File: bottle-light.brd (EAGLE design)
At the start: 88 x 88 mm, 48 parts, among them IC1 STM32F334K8T, IC2 LF33, J2 UJ2-MIBH-4-SMT-TR, U1 EC11B15242AZ, X1 78127-1128, X3 SWD

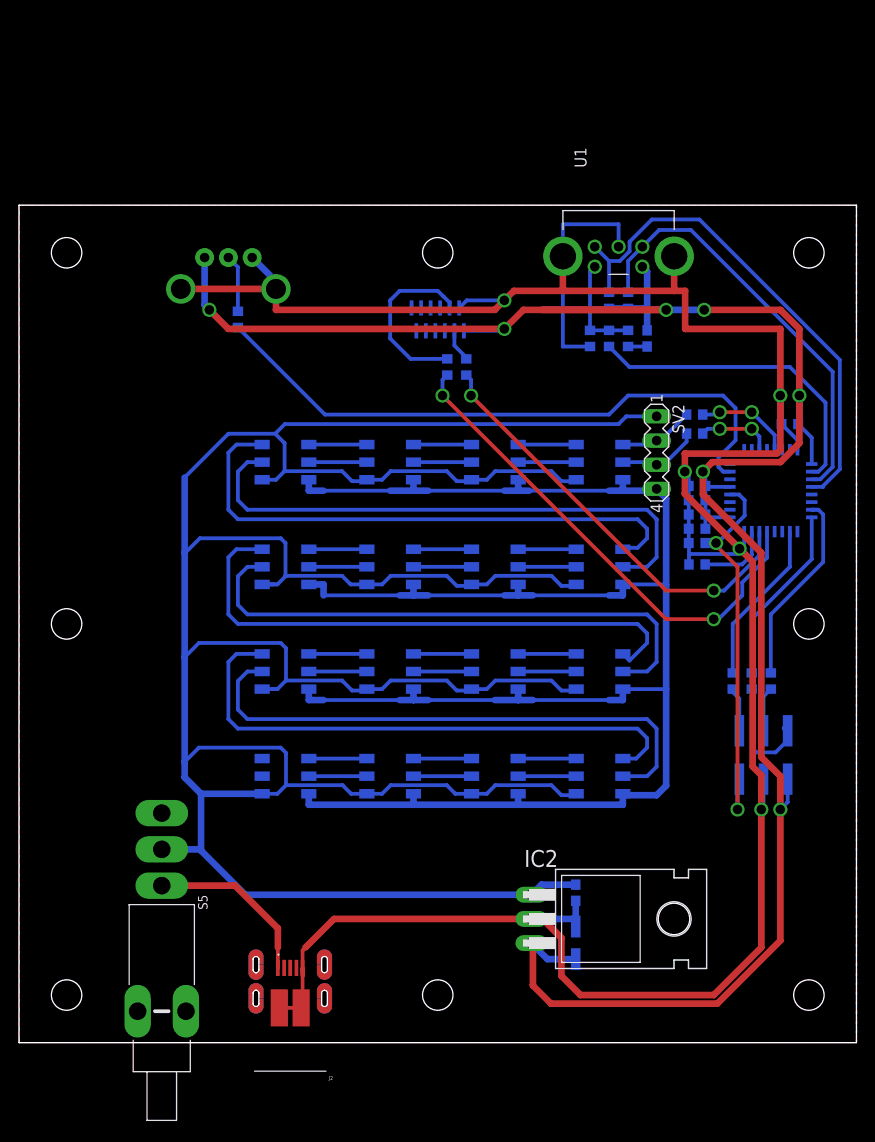
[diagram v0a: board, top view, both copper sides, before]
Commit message: v0.2.5 changed luminosity potentiometer | potentiometer and incremental encoder set to correct position
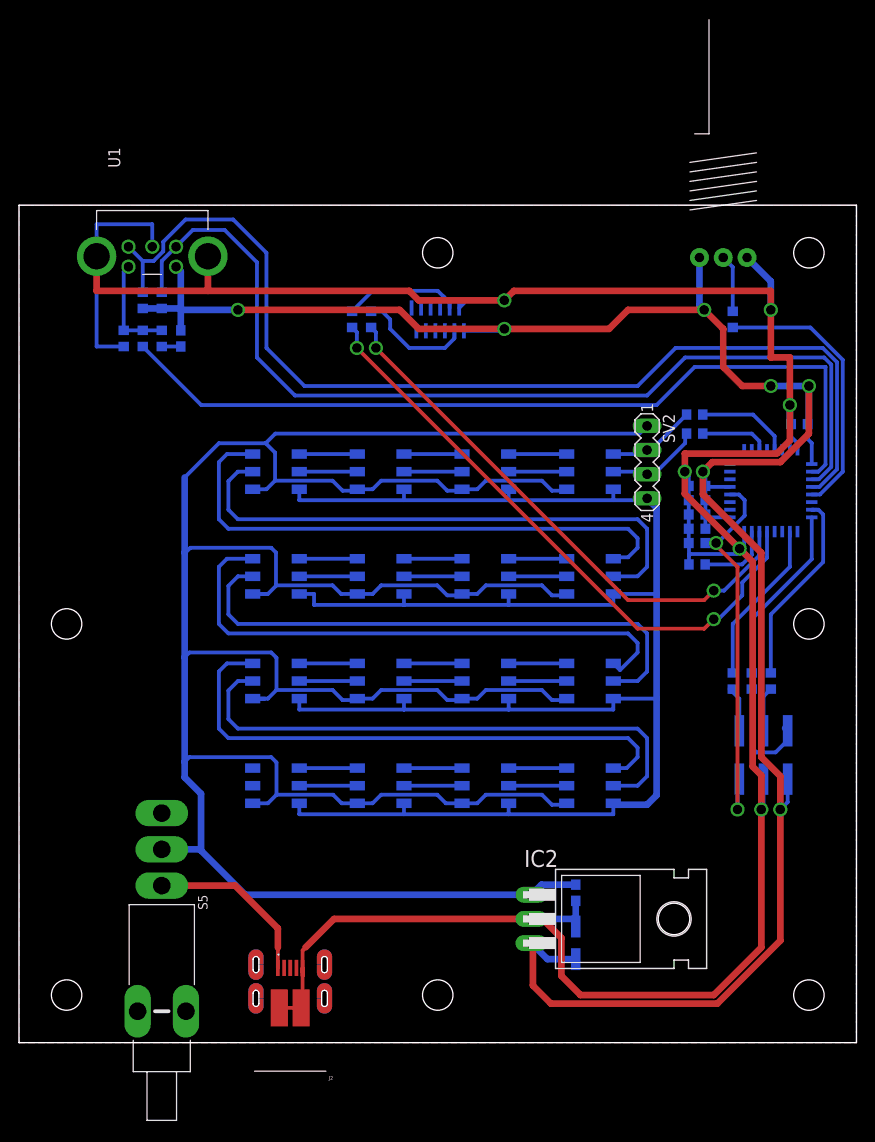
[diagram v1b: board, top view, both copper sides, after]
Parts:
- R26: device h8-rlc:RK09K -> h8-rlc:RK0971110
- moved R26 52.0 mm to (74.0, 82.5)
- moved R28 52.0 mm to (75.0, 76.0)
- moved C7 49.0 mm to (17.0, 74.0)
- moved R30 49.0 mm to (15.0, 74.0)
- moved R31 49.0 mm to (11.0, 74.0)
- moved R32 49.0 mm to (13.0, 74.0)
- moved R6 49.0 mm to (13.0, 78.0)
- moved R7 49.0 mm to (15.0, 78.0)
- moved U1 49.0 mm to (14.0, 94.0)
- moved R3 11.2 mm to (35.0, 76.0)
- moved R4 11.2 mm to (37.0, 76.0)
- moved LD1 1.41 mm to (60.0, 60.0)
- moved LD10 1.41 mm to (49.0, 38.0)
- moved LD11 1.41 mm to (38.0, 38.0)
- moved LD12 1.41 mm to (27.0, 38.0)
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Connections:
- removed net N$34: IC1.7, R28.2
- new net N$6: IC1.21, R28.2
- net GND: no longer R26.NC1, R26.NC2
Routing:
- net N$34: track 65.8 -> 0.00 mm
- net ENCODER-A: track 45.0 -> 103.4 mm
- net ENCODER-B: track 53.4 -> 110.8 mm
- net ENCODER-BUTTON: track 33.5 -> 88.0 mm
- net N$6: track 0.00 -> 29.0 mm
- net N$5: track 45.2 -> 58.1 mm
- net +5V: track 340.8 -> 328.3 mm
- net N$4: track 52.4 -> 64.3 mm
- net +3V3: track 238.8 -> 227.6 mm
- net TOUCH-I2C-SDA: track 3.47 -> 12.1 mm
- net GND: track 491.4 -> 499.9 mm, vias 5 -> 6
- net TOUCH-I2C-SCL: track 18.6 -> 12.2 mm
- net LED-SPI-MOSI: track 8.00 -> 9.42 mm
- net LED-SPI-CLK: track 8.96 -> 10.4 mm
- net N$2: track 7.89 -> 7.18 mm, vias 2 -> 0
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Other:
- board text added: "BottleLight v0.2.5 11.06.2019 HansAchterbahn MIT Licence"
- board text removed: "BottleLight v0.2.4 10.06.2019 HansAchterbahn MIT Licence"

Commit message: v0.2.6 STM32 rotated 45 degrees to optimize wire routing.
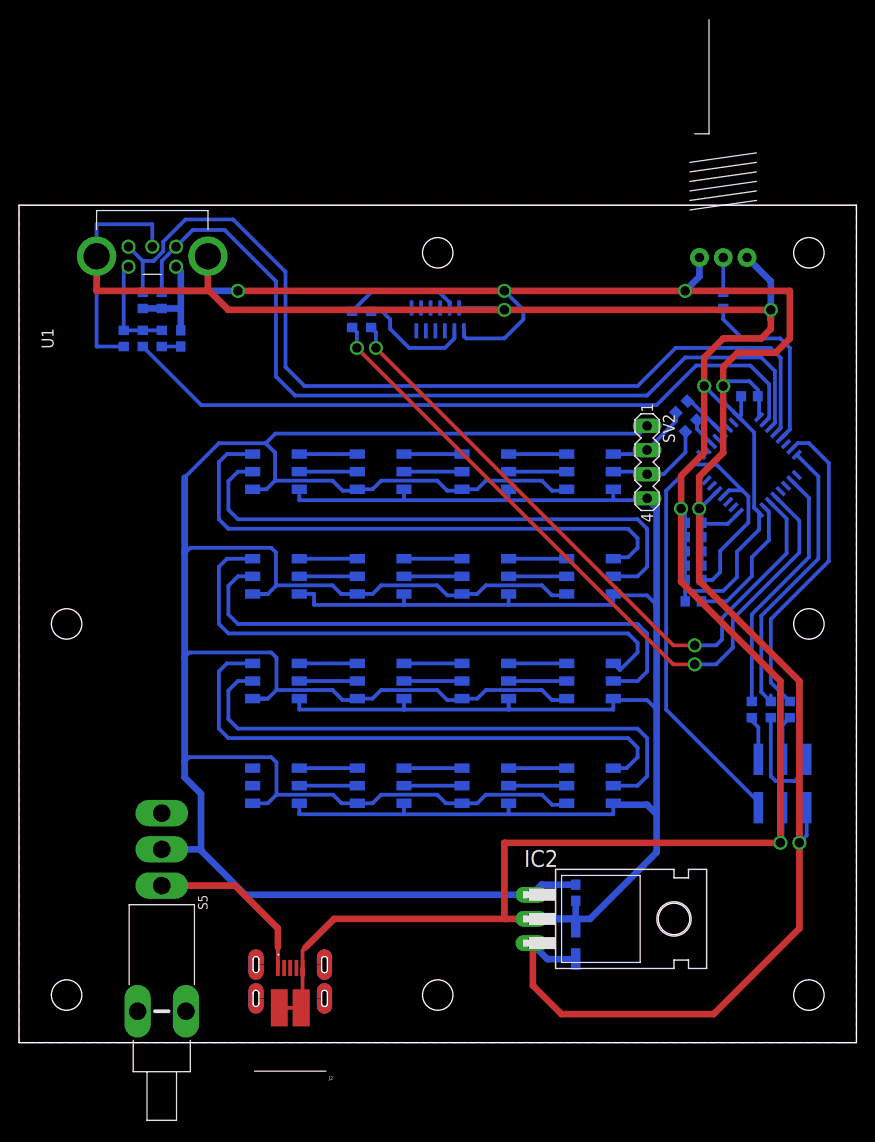
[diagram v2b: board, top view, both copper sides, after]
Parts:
- moved C3 6.01 mm to (76.8, 67.9)
- moved C5 3.90 mm to (70.9, 51.6)
- moved C1 3.90 mm to (70.9, 48.6)
- moved C2 3.90 mm to (70.9, 50.1)
- moved C4 3.90 mm to (70.9, 53.1)
- moved C6 3.90 mm to (70.9, 54.6)
- moved R19 3.90 mm to (70.9, 46.4)
- moved R20 3.61 mm to (81.0, 35.0)
- moved R21 3.61 mm to (79.0, 35.0)
- moved R22 3.61 mm to (77.0, 35.0)
- moved X3 3.61 mm to (81.5, 28.5)
- moved IC1 3.55 mm to (76.7, 60.7), turned to 135 degrees
- moved R28 2.24 mm to (74.0, 78.0)
- moved R2 1.59 mm to (69.6, 66.8), turned to 135 degrees
- moved R1 0.89 mm to (70.6, 64.8), turned to 135 degrees
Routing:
- net GND: track 499.9 -> 531.1 mm, vias 6 -> 5
- net NRST: track 40.9 -> 62.6 mm, vias 2 -> 0
- net N$24: track 20.5 -> 33.5 mm
- net ENCODER-BUTTON: track 88.0 -> 75.1 mm
- net ENCODER-A: track 103.4 -> 90.6 mm
- net ENCODER-B: track 110.8 -> 98.2 mm
- net N$4: track 64.3 -> 76.2 mm
- net N$5: track 58.1 -> 69.9 mm
- net N$1: track 19.6 -> 30.4 mm
- net N$25: track 17.3 -> 26.5 mm
- net N$6: track 29.0 -> 20.2 mm
- net +3V3: track 227.6 -> 235.9 mm, vias 7 -> 6
- net N$23: track 7.76 -> 14.6 mm
- net N$2: track 7.18 -> 3.16 mm
- net N$3: track 9.92 -> 6.54 mm
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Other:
- board text added: "BottleLight v0.2.6 11.06.2019 HansAchterbahn MIT Licence"
- board text added: "ToDo: ----- - Einschalter gegen dezenteren Typ austauschen - TouchPad anbindung überprüfen - Positionen prüfen: Anschalter, Micro-USB-Schnittstelle - VDDA Beschaltung überprüfen"
- board text removed: "BottleLight v0.2.5 11.06.2019 HansAchterbahn MIT Licence"
- board text removed: "ToDo: ----- - Poti wechseln -> an Drehencoder Dimensionen anpassen - Einschalter gegen dezenteren Typ austauschen - TouchPad anbindung überprüfen - Positionen prüfen: Poti, Drehencoder, Anschalter, Micro-USB-Schnittstelle - VDDA Beschaltung überprüfen"

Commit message: v0.2.7 new power switch | new restricted areas | optimized wires | checked positions of all components mounted at the edge | optimized polygon
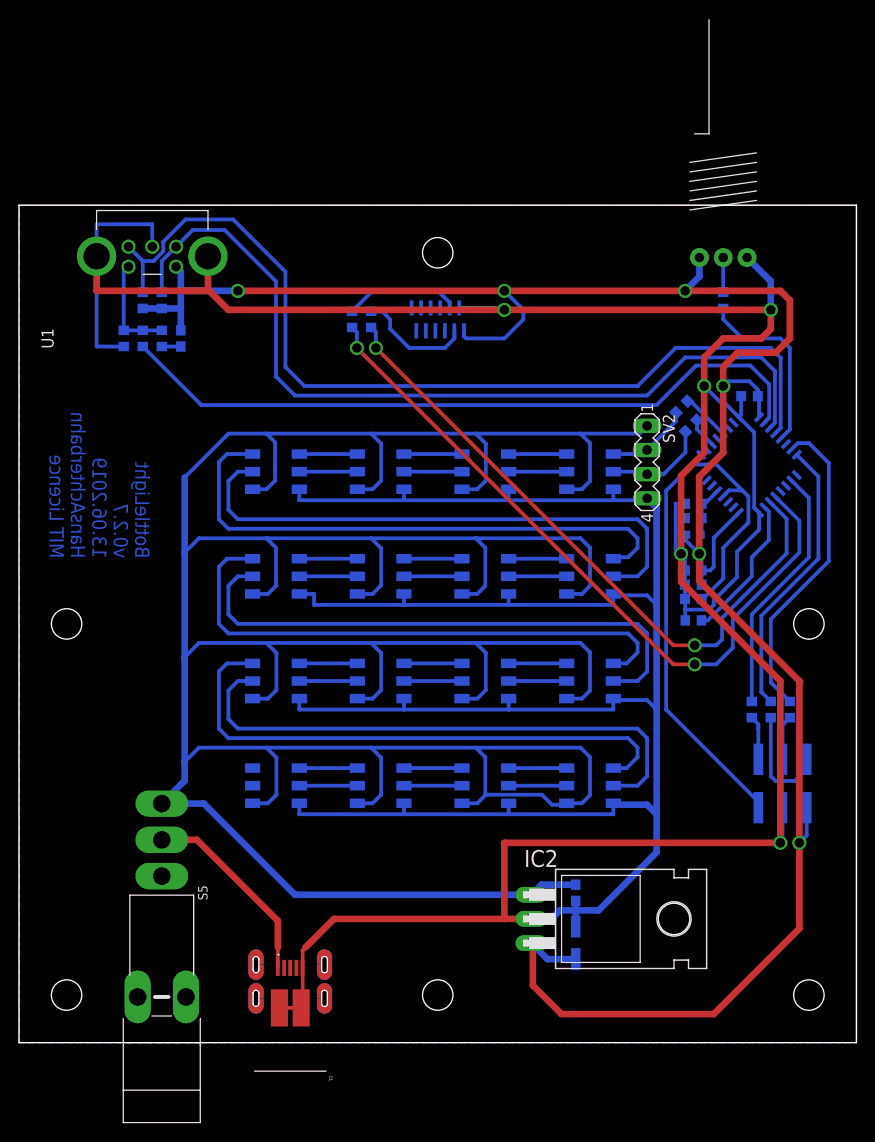
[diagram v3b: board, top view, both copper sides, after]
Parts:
- added L1: BLM18, Seeed-OPL-Inductor:L0603
- S5: value SPDT_PCB -> 300SP1J1BLKM7QE; device h8-switch:SPDT_PCB -> h8-switch:300SP1J1BLKM7QE
- moved C1 2.00 mm to (70.9, 46.6)
- moved C2 2.00 mm to (70.9, 48.1)
- moved C4 2.00 mm to (70.9, 55.1)
- moved C5 2.00 mm to (70.9, 49.6)
- moved C6 2.00 mm to (70.9, 56.6)
- moved R19 2.00 mm to (70.9, 44.4)
- moved S5 1.00 mm to (15.0, 17.5)
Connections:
- new net N$7: C4.1, C6.1, IC1.5, L1.2
- net +3V3: now also L1.1; no longer C4.1, C6.1, IC1.5
- net +5V: now also S5.3; no longer S5.2
- net 5V-IN: now also S5.2; no longer S5.1
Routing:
- net +5V: track 328.3 -> 401.5 mm
- net N$7: track 0.00 -> 5.50 mm
- net 5V-IN: track 18.2 -> 20.7 mm
- net GND: track 531.1 -> 528.9 mm
- net N$3: track 6.54 -> 5.11 mm
- net NRST: track 62.6 -> 63.7 mm
- net N$6: track 20.2 -> 19.3 mm
- net N$23: track 14.6 -> 15.4 mm
- net N$1: track 30.4 -> 29.8 mm
- net N$53: track 59.3 -> 58.8 mm
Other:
- board text added: "BottleLight v0.2.7 13.06.2019 HansAchterbahn MIT Licence"
- board text added: "ToDo: ----- - Names und Values ausrichten"
- board text removed: "BottleLight v0.2.6 11.06.2019 HansAchterbahn MIT Licence"
- board text removed: "ToDo: ----- - Einschalter gegen dezenteren Typ austauschen - TouchPad anbindung überprüfen - Positionen prüfen: Anschalter, Micro-USB-Schnittstelle - VDDA Beschaltung überprüfen"

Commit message: optimized text positions | added 2 jumpers for easy usage of additional LED strip
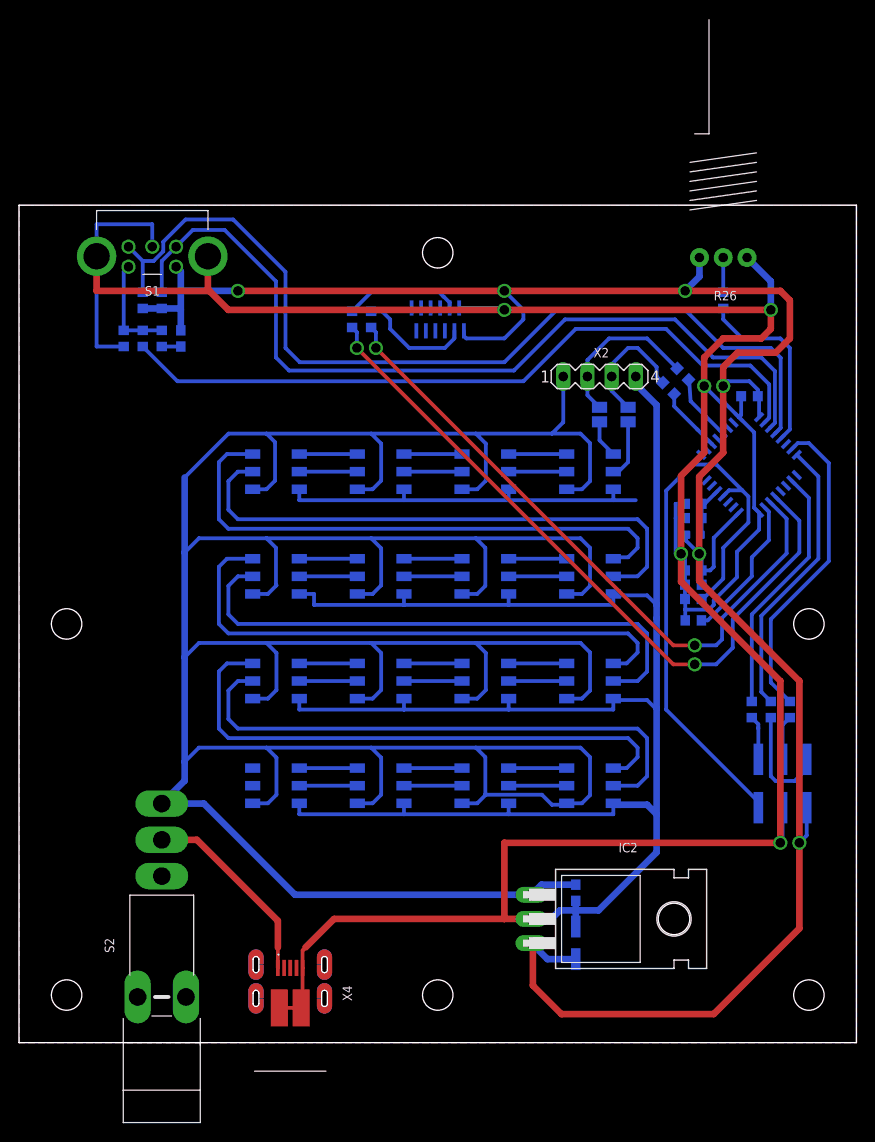
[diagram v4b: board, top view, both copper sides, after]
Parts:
- removed SV2: (no value), con-lstb:MA04-1
- added J1: (no value), jumper:SJ
- added X2: (no value), con-lstb:MA04-1
- added X4: UJ2-MIBH-4-SMT-TR, UJ2-MIBH-4-SMT-TR:CUIINC_UJ2-MIBH-4-SMT-TR-2
- J2: value UJ2-MIBH-4-SMT-TR -> (none); device UJ2-MIBH-4-SMT-TR:CUIINC_UJ2-MIBH-4-SMT-TR-2 -> jumper:SJ
- moved J2 71.8 mm to (61.0, 66.0), flipped to the bottom, turned to 270 degrees
- moved R1 4.61 mm to (68.2, 68.8), turned to 225 degrees
- moved R2 3.44 mm to (69.8, 70.2), turned to 225 degrees
- renumbered S5 to S2, U1 to S1
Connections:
- new net N$8: J1.2, LD1.2
- new net N$9: J2.2, LD1.1
- net +5V: now also X2.1; no longer SV2.1
- net 5V-IN: now also X4.1; no longer J2.1
- net GND: now also X2.4, X4.5, X4.P5, X4.P6; no longer J2.5, J2.P5, J2.P6, SV2.4
- net LED-SPI-CLK: now also J1.1, X2.3; no longer LD1.2, SV2.3
- net LED-SPI-MOSI: now also J2.1, X2.2; no longer LD1.1, SV2.2
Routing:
- net GND: track 528.9 -> 540.9 mm
- net LED-SPI-MOSI: track 8.92 -> 17.2 mm
- net N$8: track 0.00 -> 6.20 mm
- net N$9: track 0.00 -> 3.99 mm
- net N$2: track 3.16 -> 6.89 mm
- net LED-SPI-CLK: track 10.8 -> 13.4 mm
- net N$3: track 5.11 -> 7.14 mm
- net ENCODER-BUTTON: track 75.1 -> 76.4 mm
- net +5V: track 401.5 -> 400.7 mm
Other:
- board text removed: "ToDo: ----- - Names und Values ausrichten"

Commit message: Vias verkleinert | 3D Modelle hinzugefügt | auf Fusion gepusht
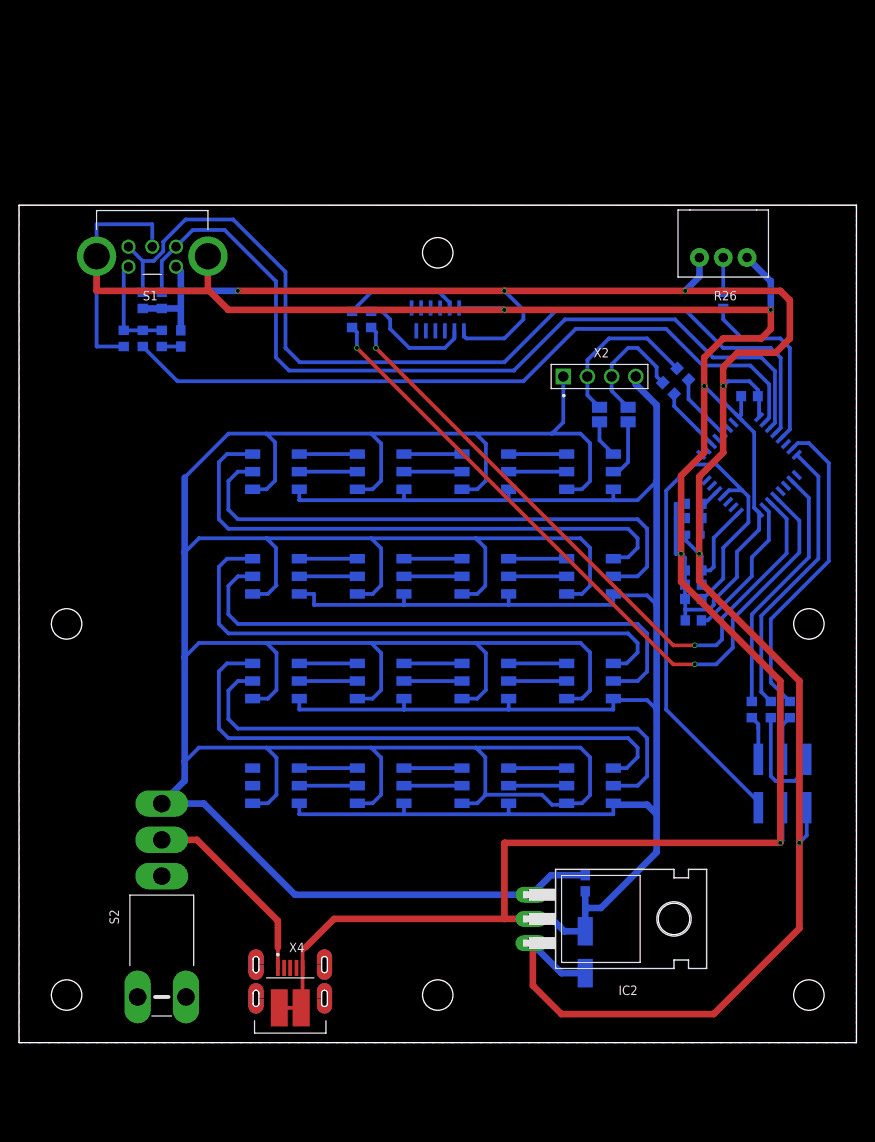
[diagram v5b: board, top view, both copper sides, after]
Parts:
- C13: device rcl:UD-5X5,8_NICHICON -> rcl:153CLV-0505
- LD1, LD10, LD11, LD12, LD13, LD14, LD15, LD16, LD2, LD3, LD4, LD5, LD6, LD7, LD8, LD9: device 3587:APA102C-5050 -> h8-optic:APA102C-5050
- S1: device EC11B15242AZ:EC11B15242AZ -> h8-switch:EC11B15242AZ
- X1: device SamaSys:781271128 -> h8-conector:781271128
- X2: value (none) -> 61300411121; device con-lstb:MA04-1 -> Headers:61300411121
- moved C12 1.41 mm to (59.5, 16.8)
- moved C13 1.41 mm to (59.5, 9.50)
- moved X4 1.00 mm to (28.5, 1.00)
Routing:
- net GND: track 540.9 -> 549.2 mm
- net +3V3: track 235.9 -> 237.5 mm
- net +5V: track 400.7 -> 402.0 mm
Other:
- board text added: "BottleLight v0.2.7 27.06.2019 HansAchterbahn MIT Licence"
- board text removed: "BottleLight v0.2.7 13.06.2019 HansAchterbahn MIT Licence"
